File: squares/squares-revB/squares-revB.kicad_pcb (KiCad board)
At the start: 2 copper layers, 113.3 x 75.4 mm, 108 parts, among them J1 USB_C_Pwr, J10 Line In, J11 AND, J12 Mix_In, J13 Mix/Line Out, J14 VCA, J15 Filter, J2 Mux In, J3 Mux Sel, J4 ISP, J5 Square Out Hi, J6 Square Out Lo, J7 Sig Out, J8 Line OUT, J9 Line IN, Q1 2N3906, U1 74HC00, U2 40106, U3 74HC00, U4 74HC00, U5 ATtiny2313-20P, U7 MCP602

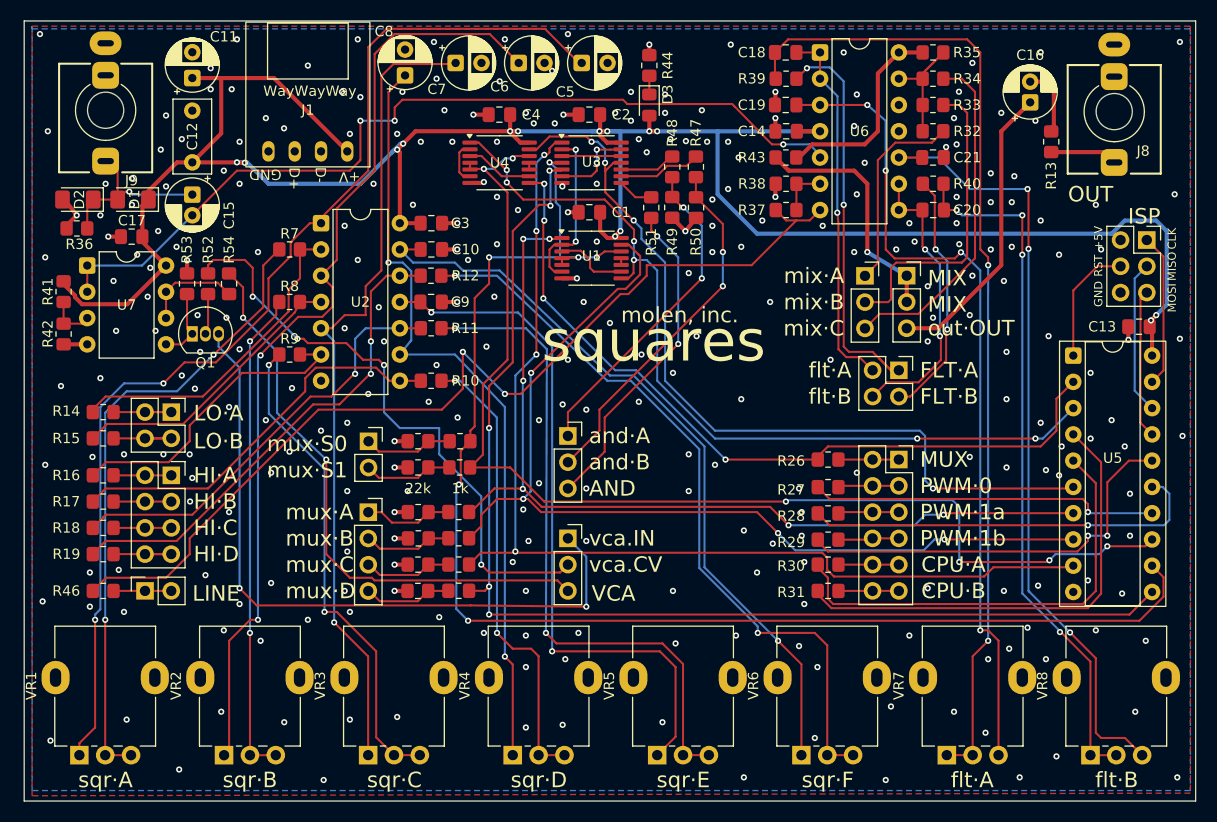
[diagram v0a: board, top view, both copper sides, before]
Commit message: squares: added revB board; added playground firmware
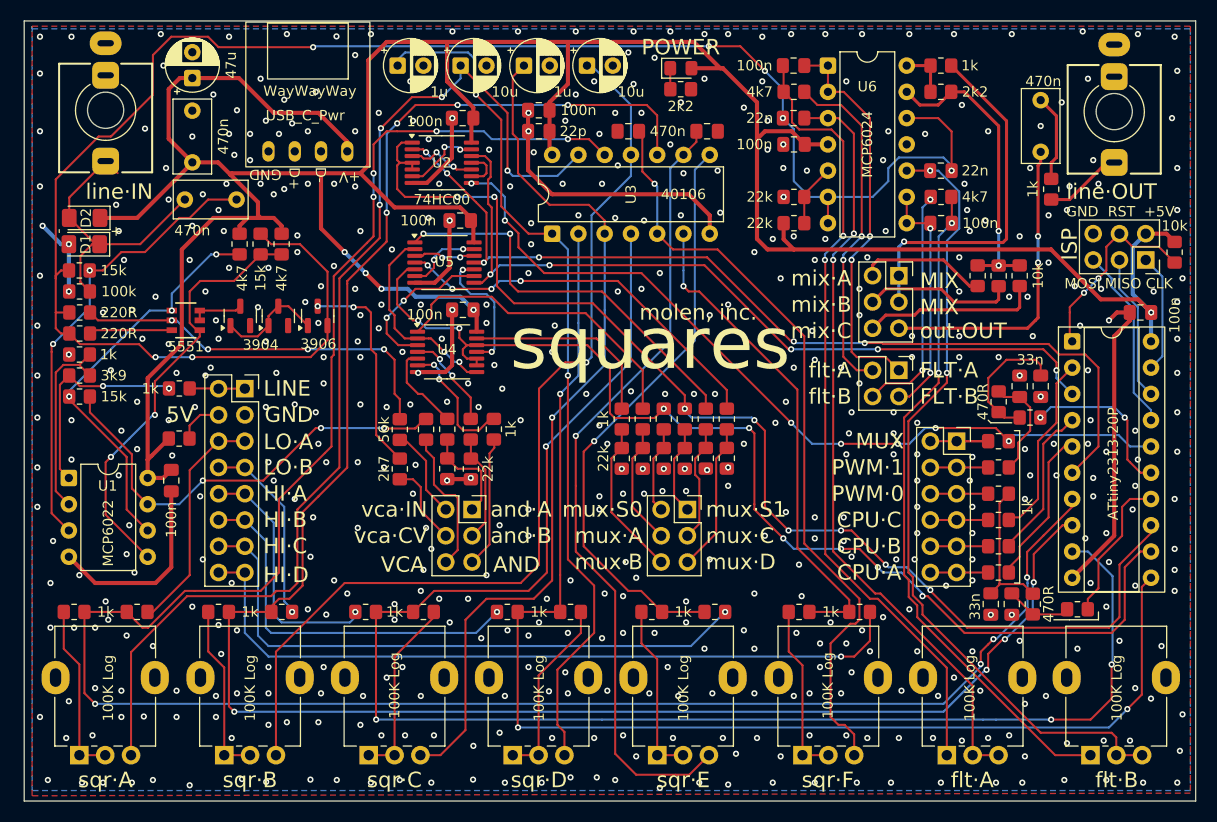
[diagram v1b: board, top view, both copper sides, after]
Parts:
- removed the J10 at (91.4, 75.7)
- removed J11: AND, Connector_PinSocket_2.54mm:PinSocket_1x03_P2.54mm_Vertical
- removed J12: Mix_In, Connector_PinSocket_2.54mm:PinSocket_1x03_P2.54mm_Vertical
- removed J13: Mix/Line Out, Connector_PinSocket_2.54mm:PinSocket_1x03_P2.54mm_Vertical
- removed J14: VCA, Connector_PinSocket_2.54mm:PinSocket_1x03_P2.54mm_Vertical
- removed the J2 at (113.0, 68.1)
- removed the J6 at (94.0, 58.4)
- removed the R2 at (121.8, 70.6)
- removed the R20 at (117.8, 63.8)
- removed the R21 at (117.8, 61.2)
- removed the R25 at (117.9, 68.1)
- removed the R5 at (121.9, 61.2)
- removed the U7 at (85.9, 44.2)
- added C11: 100n, Capacitor_SMD:C_0805_2012Metric_Pad1.18x1.45mm_HandSolder, F.Cu at (129.5, 29.2)
- added C21: 33n, Capacitor_SMD:C_0805_2012Metric_Pad1.18x1.45mm_HandSolder, F.Cu at (178.1, 55.9)
- added C22: 33n, Capacitor_SMD:C_0805_2012Metric_Pad1.18x1.45mm_HandSolder, F.Cu at (176.0, 55.9)
- added C25: 33n, Capacitor_SMD:C_0805_2012Metric_Pad1.18x1.45mm_HandSolder, F.Cu at (175.3, 77.0)
- added C26: 33n, Capacitor_SMD:C_0805_2012Metric_Pad1.18x1.45mm_HandSolder, F.Cu at (173.2, 77.0)
- added J4: VCA, Connector_PinSocket_2.54mm:PinSocket_2x03_P2.54mm_Vertical, F.Cu at (123.1, 67.8)
- added J7: MUX, Connector_PinSocket_2.54mm:PinSocket_2x03_P2.54mm_Vertical, F.Cu at (143.9, 67.8)
- added Q2: 3904, Package_TO_SOT_SMD:SOT-23, F.Cu at (104.3, 49.1)
- added Q3: 3904, Package_TO_SOT_SMD:SOT-23, F.Cu at (100.7, 49.1)
- added Q4: 3906, Package_TO_SOT_SMD:SOT-23, F.Cu at (108.1, 49.1)
- added R10: 15k, Resistor_SMD:R_0805_2012Metric_Pad1.20x1.40mm_HandSolder, F.Cu at (102.6, 42.1)
- added R11: 22k, Resistor_SMD:R_0805_2012Metric_Pad1.20x1.40mm_HandSolder, F.Cu at (94.7, 61.0)
- added R12: 4k7, Resistor_SMD:R_0805_2012Metric_Pad1.20x1.40mm_HandSolder, F.Cu at (104.6, 42.1)
- added R18: 1k, Resistor_SMD:R_0805_2012Metric_Pad1.20x1.40mm_HandSolder, F.Cu at (139.6, 59.1)
- added R19: 1k, Resistor_SMD:R_0805_2012Metric_Pad1.20x1.40mm_HandSolder, F.Cu at (137.5, 59.1)
- added R22: 22k, Resistor_SMD:R_0805_2012Metric_Pad1.20x1.40mm_HandSolder, F.Cu at (139.6, 62.9)
- added R24: 22k, Resistor_SMD:R_0805_2012Metric_Pad1.20x1.40mm_HandSolder, F.Cu at (137.5, 62.9)
- added R3: 15k, Resistor_SMD:R_0805_2012Metric_Pad1.20x1.40mm_HandSolder, F.Cu at (85.1, 44.7)
- added R39: 22k, Resistor_SMD:R_0805_2012Metric_Pad1.20x1.40mm_HandSolder, F.Cu at (141.6, 62.9)
- added R4: 220R, Resistor_SMD:R_0805_2012Metric_Pad1.20x1.40mm_HandSolder, F.Cu at (85.1, 48.8)
- added R40: 1k, Resistor_SMD:R_0805_2012Metric_Pad1.20x1.40mm_HandSolder, F.Cu at (141.6, 59.1)
- added R55: 470R, Resistor_SMD:R_0805_2012Metric_Pad1.20x1.40mm_HandSolder, F.Cu at (177.0, 58.9)
- added R56: 470R, Resistor_SMD:R_0805_2012Metric_Pad1.20x1.40mm_HandSolder, F.Cu at (174.0, 57.4)
- added R58: 10k, Resistor_SMD:R_0805_2012Metric_Pad1.20x1.40mm_HandSolder, F.Cu at (191.0, 42.9)
- added R62: 470R, Resistor_SMD:R_0805_2012Metric_Pad1.20x1.40mm_HandSolder, F.Cu at (177.3, 77.0)
- added R64: 470R, Resistor_SMD:R_0805_2012Metric_Pad1.20x1.40mm_HandSolder, F.Cu at (181.6, 77.5)
- added R7: 15k, Resistor_SMD:R_0805_2012Metric_Pad1.20x1.40mm_HandSolder, F.Cu at (85.1, 56.9)
- added R9: 4k7, Resistor_SMD:R_0805_2012Metric_Pad1.20x1.40mm_HandSolder, F.Cu at (100.6, 42.1)
- added U1: MCP6022, Package_DIP:DIP-8_W7.62mm, F.Cu at (84.1, 64.8)
- C10: renamed from C4; value 100n -> 22p
- C16: renamed from C9; value 100n -> 470n
- C18: value 22n -> 100n
- C19: renamed from C16; value 10u BP -> 470n; footprint Capacitor_THT:CP_Radial_D5.0mm_P2.00mm -> Capacitor_THT:C_Rect_L7.0mm_W3.5mm_P5.00mm
- C2: renamed from C15; value 10u BP -> 470n; footprint Capacitor_THT:CP_Radial_D5.0mm_P2.00mm -> Capacitor_THT:C_Rect_L7.0mm_W3.5mm_P5.00mm
- C24: renamed from C20; value 22n -> 100n
- C9: renamed from C10; value 100n -> 470n
- D3: value LED -> POWER
- J3: value Mux Sel -> Inputs; footprint Connector_PinSocket_2.54mm:PinSocket_1x02_P2.54mm_Vertical -> Connector_PinSocket_2.54mm:PinSocket_2x08_P2.54mm_Vertical
- J5: value Square Out Hi -> MIX; footprint Connector_PinSocket_2.54mm:PinSocket_2x04_P2.54mm_Vertical -> Connector_PinSocket_2.54mm:PinSocket_2x03_P2.54mm_Vertical
- Q1: value 2N3906 -> DMMT5551; footprint Package_TO_SOT_THT:TO-92_Inline -> DMMT5551:SOIC6_DMMT551_DIO
- R1: value 1k -> 220R
- R20: renamed from R52; value 10k -> 56k
- R31: renamed from R53; value 1k -> 2k7
- R34: renamed from R39; value 100k -> 4k7
- R50: renamed from R40; value 100k -> 4k7
- U6: value ~ -> MCP6024
- moved R47 73.4 mm to (160.5, 77.7)
- moved J5 73.0 mm to (164.3, 45.2)
- moved R33 71.9 mm to (154.2, 37.6), turned to 180 degrees
- moved R42 70.9 mm to (154.2, 40.1), turned to 180 degrees
- moved R5 70.3 mm to (85.1, 52.8)
- moved R2 70.2 mm to (85.1, 54.9)
- moved R48 59.7 mm to (146.5, 77.7)
- moved R46 48.2 mm to (154.7, 77.7), turned to 180 degrees
- moved R8 40.8 mm to (84.6, 77.7)
- moved R1 40.5 mm to (85.1, 50.8)
- moved R30 40.5 mm to (126.5, 77.7), turned to 0 degrees
- moved R26 35.0 mm to (120.7, 60.1)
- moved R28 34.9 mm to (120.7, 63.9)
- moved R45 34.8 mm to (140.4, 77.7), turned to 180 degrees
- moved R43 32.5 mm to (147.7, 62.9), turned to 90 degrees
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- renumbered C12 to C1, C2 to C12, C1 to C13, C3 to C14, C19 to C15, C14 to C17, C21 to C20, C13 to C23, C11 to C3, C17 to C4, C6 to C5, C7 to C6, C8 to C7, C5 to C8, D2 to D1, D1 to D2, J9 to J1, J7 to J10, J1 to J2, J15 to J6, J4 to J9, R46 to R13, R15 to R14, R16 to R15, R8 to R16, R14 to R17, R37 to R2, R51 to R21, R48 to R23, R54 to R25, R47 to R26, R10 to R27, R50 to R28, R49 to R29, R17 to R30, R9 to R32, R42 to R33, R44 to R35, R6 to R36, R3 to R37, R23 to R38, R24 to R41, R41 to R42, R22 to R43, R4 to R44, R11 to R45, R12 to R46, R19 to R47, R18 to R48, R13 to R49, R38 to R5, R43 to R51, R35 to R52, R33 to R53, R32 to R54, R34 to R57, R26 to R59, R36 to R6, R28 to R60, R27 to R61, R29 to R63, R30 to R65, R31 to R66, R7 to R8, U4 to U2, U2 to U3, U1 to U4, U3 to U5, U5 to U7
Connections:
- net Net-(J11-Pin_1) renamed AND_b
- net Net-(J11-Pin_2) renamed AND_a
- C15 pad 1: GND -> REF_2.5v
- C16 pad 2: Net-(C9-Pad2) -> Net-(C16-Pad2)
- C2 pad 2: REF_2.5v -> Net-(U1A-+)
- C20 pad 1: GND -> REF_2.5v
- C24 pad 1: Net-(C20-Pad1) -> Net-(C24-Pad1)
- C5 pad 1: Net-(C6-Pad1) -> Net-(C5-Pad1)
- C6 pad 1: Net-(C7-Pad1) -> Net-(C6-Pad1)
- C7 pad 1: Net-(C8-Pad1) -> Net-(C7-Pad1)
- C8 pad 1: Net-(C5-Pad1) -> Net-(C8-Pad1)
- C9 pad 2: Net-(C10-Pad2) -> Net-(C9-Pad2)
- J3 pad 2: Net-(J3-Pin_2) -> Net-(J3-Pin_1)
- J5 pad 2: Net-(J5-Pin_1) -> MIX_In_A
- J5 pad 3: Net-(J5-Pin_3) -> Net-(J5-Pin_1)
- J5 pad 4: Net-(J5-Pin_3) -> MIX_In_B
- J5 pad 5: Net-(J5-Pin_5) -> LINE_Out
- J5 pad 6: Net-(J5-Pin_5) -> MIX_In_C
- J6 pad 1: FILT_A_In -> FILT_A_Out
- J6 pad 2: FILT_A_Out -> FILT_A_In
- J6 pad 3: FILT_B_In -> FILT_B_Out
- J6 pad 4: FILT_B_Out -> FILT_B_In
- Q1 pad 1: Net-(Q1-E) -> Net-(U1B--)
- Q1 pad 3: VCA_in -> Net-(Q1-Pad3)
- R1 pad 1: MUX_In_A -> Net-(Q1-Pad3)
- R1 pad 2: Net-(J2-Pin_1) -> REF_2.5v
- R13 pad 2: Net-(J10-Pin_1) (its old number) -> Net-(J3-Pin_1)
- R14 pad 1: Net-(J6-Pin_3) -> Net-(J3-Pin_7)
- R15 pad 1: Net-(J5-Pin_1) -> Net-(J3-Pin_10)
- R16 pad 2: Net-(R8-Pad2) -> Net-(R16-Pad2)
- R17 pad 1: Net-(J6-Pin_1) -> Net-(J3-Pin_5)
- R2 pad 2: Net-(U6B--) -> Net-(U1A--)
- R20 pad 2: VCA_cv -> VCA_in
- R21 pad 1: Net-(J11-Pin_3) -> AND_out
- R21 pad 2: Net-(R51-Pad2) -> Net-(R21-Pad2)
- R23 pad 1: Net-(R48-Pad1) -> Net-(R23-Pad1)
- R26 pad 1: Net-(R47-Pad1) -> Net-(R26-Pad1)
- R27 pad 2: Net-(R10-Pad2) -> Net-(R27-Pad2)
- R30 pad 1: Net-(J5-Pin_3) -> Net-(J3-Pin_11)
- R31 pad 1: Net-(Q1-E) -> VCA_cv
- R31 pad 2: GND -> Net-(Q4-E)
- R32 pad 2: Net-(R9-Pad2) -> Net-(R32-Pad2)
- R33 pad 1: Net-(U7A-+) -> Net-(U6B-+)
- R36 pad 2: Net-(J3-Pin_2) -> Net-(J7-Pin_1)
- R41 pad 2: Net-(J2-Pin_2) -> Net-(J7-Pin_1)
- R42 pad 1: Net-(U7A-+) -> Net-(U6B-+)
- R45 pad 2: Net-(R11-Pad2) -> Net-(R45-Pad2)
- R46 pad 2: Net-(R12-Pad2) -> Net-(R46-Pad2)
- R47 pad 1: Net-(J5-Pin_7) -> Net-(J3-Pin_15)
- R48 pad 1: Net-(J5-Pin_5) -> Net-(J3-Pin_13)
- R5 pad 2: Net-(U6B--) -> Net-(U1A--)
- R50 pad 1: Net-(C20-Pad1) -> Net-(C24-Pad1)
- R51 pad 2: Net-(J13-Pin_1) -> Net-(J5-Pin_1)
- R60 pad 2: CPU_PWM_1A -> CPU_PWM_0
- R61 pad 2: CPU_PWM_0 -> CPU_PWM_1
- R63 pad 2: CPU_PWM_1B -> CPU_Out_C
- R65 pad 2: CPU_Out_A -> CPU_Out_B
- R66 pad 2: CPU_Out_B -> CPU_Out_A
- R8 pad 2: Net-(R7-Pad2) -> Net-(R8-Pad2)
- U2 pad 1: MUX_Partial_AB -> MUX_Sel1
- U2 pad 10: Net-(U4-Pad10) -> Net-(U2-Pad10)
- U2 pad 11: Net-(U4-Pad10) -> Net-(U2-Pad11)
- U2 pad 12: MUX_Sel1 -> MUX_Partial_AB
- U2 pad 13: MUX_Partial_CD -> Net-(U2-Pad13)
- U2 pad 2: Net-(U4-Pad2) -> MUX_Partial_CD
- U2 pad 3: Net-(U4-Pad3) -> Net-(U2-Pad10)
- U2 pad 6: Net-(U4-Pad2) -> Net-(U2-Pad13)
- U2 pad 9: Net-(U4-Pad3) -> Net-(U2-Pad11)
- U3 pad 1: Net-(C5-Pad1) -> Net-(C7-Pad1)
- U3 pad 10: SqrE_Out -> SqrB_Out
- U3 pad 11: Net-(C9-Pad2) -> Net-(C5-Pad1)
- U3 pad 12: SqrF_Out -> SqrA_Out
- U3 pad 13: Net-(C10-Pad2) -> Net-(C8-Pad1)
- U3 pad 2: SqrA_Out -> SqrD_Out
- U3 pad 4: SqrB_Out -> SqrC_Out
- U3 pad 5: Net-(C7-Pad1) -> Net-(C9-Pad2)
- U3 pad 6: SqrC_Out -> SqrF_Out
- U3 pad 8: SqrD_Out -> SqrE_Out
- U3 pad 9: Net-(C8-Pad1) -> Net-(C16-Pad2)
- U4 pad 10: Net-(U1-Pad10) -> MUX_Sel0
- U4 pad 11: Net-(U1-Pad10) -> Net-(U4-Pad11)
- U4 pad 2: Net-(U1-Pad2) -> Net-(U4-Pad2)
- U4 pad 3: Net-(U1-Pad3) -> Net-(U4-Pad3)
- U4 pad 4: MUX_Sel0 -> Net-(R23-Pad1)
- U4 pad 5: MUX_Sel0 -> Net-(R26-Pad1)
- U4 pad 6: Net-(U1-Pad2) -> Net-(R21-Pad2)
- U4 pad 8: MUX_Partial_AB -> Net-(U4-Pad2)
- U4 pad 9: Net-(U1-Pad3) -> MUX_Sel0
- U5 pad 10: Net-(R48-Pad1) -> Net-(U4-Pad11)
- U5 pad 2: Net-(U1-Pad2) -> Net-(U4-Pad2)
- U5 pad 4: MUX_Sel0 -> MUX_In_D
- U5 pad 5: MUX_In_D -> MUX_Sel0
- U5 pad 8: Net-(R51-Pad2) -> MUX_Partial_AB
- U5 pad 9: Net-(R47-Pad1) -> Net-(U4-Pad3)
- U6 pad 12: GND -> REF_2.5v
- U6 pad 5: REF_2.5v -> Net-(U6B-+)
- U6 pad 6: Net-(U6B--) -> REF_2.5v
- U6 pad 7: LINE_In -> REF_2.5v
- U7 pad 11: MUX_In_D -> SqrD_Out
- U7 pad 14: CPU_PWM_0 -> Net-(U7-PB2)
- U7 pad 15: CPU_PWM_1A -> Net-(U7-PB3)
- U7 pad 16: CPU_PWM_1B -> MUX_Out
- U7 pad 2: MUX_Out -> CPU_Out_C
- U7 pad 7: MUX_In_A -> SqrA_Out
- U7 pad 8: MUX_In_B -> SqrB_Out
- U7 pad 9: MUX_In_C -> SqrC_Out
- VR1 pad 1: Net-(C5-Pad1) -> Net-(R8-Pad2)
- VR1 pad 2: Net-(R7-Pad2) -> Net-(R8-Pad2)
- VR1 pad 3: Net-(R7-Pad2) -> Net-(C8-Pad1)
- VR2 pad 1: Net-(C6-Pad1) -> Net-(R16-Pad2)
- VR2 pad 2: Net-(R8-Pad2) -> Net-(R16-Pad2)
- VR2 pad 3: Net-(R8-Pad2) -> Net-(C5-Pad1)
- VR3 pad 1: Net-(C7-Pad1) -> Net-(R32-Pad2)
- VR3 pad 2: Net-(R9-Pad2) -> Net-(R32-Pad2)
- VR3 pad 3: Net-(R9-Pad2) -> Net-(C6-Pad1)
- VR4 pad 1: Net-(C8-Pad1) -> Net-(R27-Pad2)
- VR4 pad 2: Net-(R10-Pad2) -> Net-(R27-Pad2)
- VR4 pad 3: Net-(R10-Pad2) -> Net-(C7-Pad1)
- VR5 pad 1: Net-(C9-Pad2) -> Net-(R46-Pad2)
- VR5 pad 2: Net-(R11-Pad2) -> Net-(R46-Pad2)
- VR5 pad 3: Net-(R11-Pad2) -> Net-(C9-Pad2)
- VR6 pad 1: Net-(C10-Pad2) -> Net-(R45-Pad2)
- VR6 pad 2: Net-(R12-Pad2) -> Net-(R45-Pad2)
- VR6 pad 3: Net-(R12-Pad2) -> Net-(C16-Pad2)
- VR7 pad 2: Net-(C18-Pad1) -> Net-(U6A-+)
- VR8 pad 1: Net-(C20-Pad1) -> Net-(C24-Pad1)
- VR8 pad 2: Net-(C20-Pad1) -> Net-(U6C-+)
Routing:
- net SqrA_Out: track 31.6 -> 207.2 mm, vias 0 -> 8
- net SqrB_Out: track 27.7 -> 189.5 mm, vias 0 -> 8
- net SqrC_Out: track 30.0 -> 153.5 mm, vias 0 -> 4
- net REF_2.5v: track 85.5 -> 180.2 mm, vias 3 -> 7
- net SqrD_Out: track 38.4 -> 125.9 mm, vias 0 -> 3
- net Net-(C16-Pad2): track 0.00 -> 77.3 mm, vias 0 -> 1
- net MUX_In_D: track 114.6 -> 37.7 mm, vias 5 -> 4
- net MUX_In_B: track 95.2 -> 19.4 mm, vias 4 -> 0
- net +5V: track 228.4 -> 303.2 mm, vias 14 -> 5
- net LINE_In: track 94.9 -> 21.1 mm
- net GND: track 38.8 -> 112.5 mm, vias 285 -> 525
- net Net-(J3-Pin_15): track 0.00 -> 73.2 mm, vias 0 -> 1
- net Net-(C10-Pad2): track 72.9 -> 0.00 mm, vias 1 -> 0
- net Net-(R12-Pad2): track 72.2 -> 0.00 mm, vias 2 -> 0
- net Net-(C20-Pad1): track 67.8 -> 0.00 mm, vias 4 -> 0
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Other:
- board text added: "+"
- board text added: "-"
- board text added: "5V"
- board text added: "CPU·C"
- board text added: "PWM·1"
- board text added: "let's try that again"
- board text added: "line·IN"
- board text added: "line·OUT"
- board text added: "rev·B"
- board text added: "vca·CV"
- board text added: "vca·IN"
- board text removed: "OUT"
- board text removed: "PWM·1a"
- board text removed: "PWM·1b"
- board text removed: "vca.CV"
- board text removed: "vca.IN"

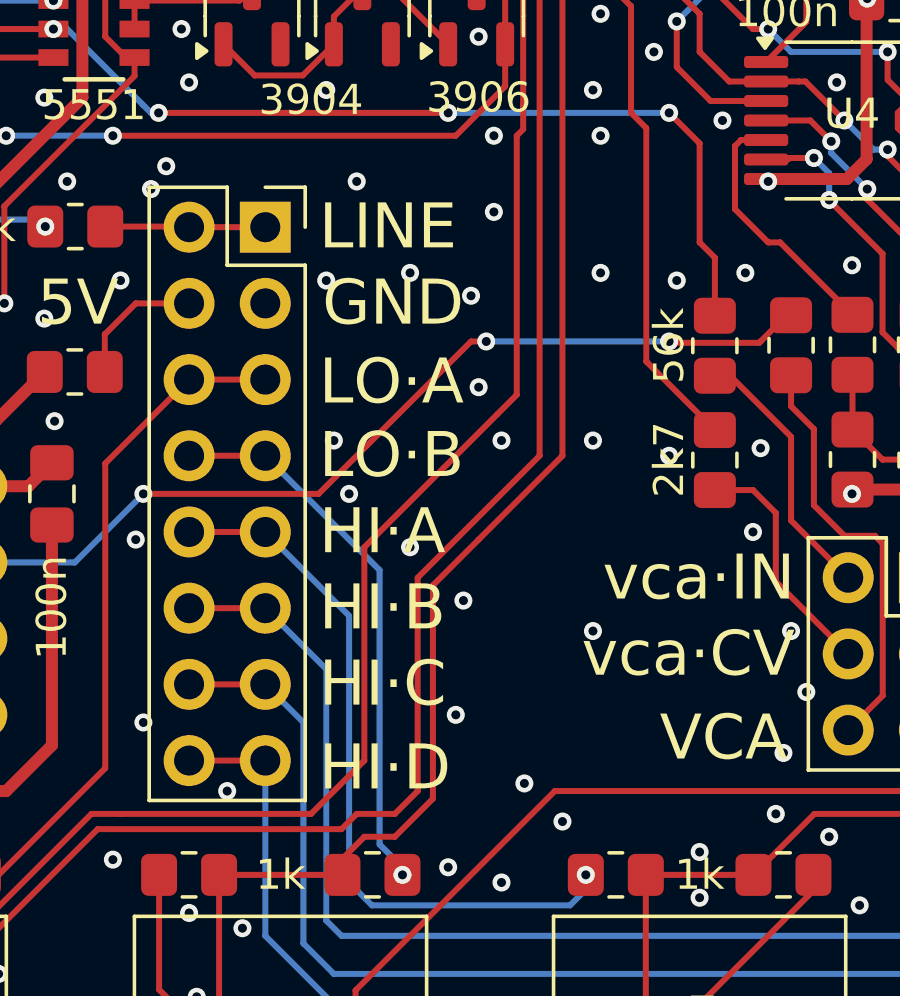
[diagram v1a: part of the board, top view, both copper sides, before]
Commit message: [squares] PWM_A is now lil percussive env triggered by MUX_Sel0
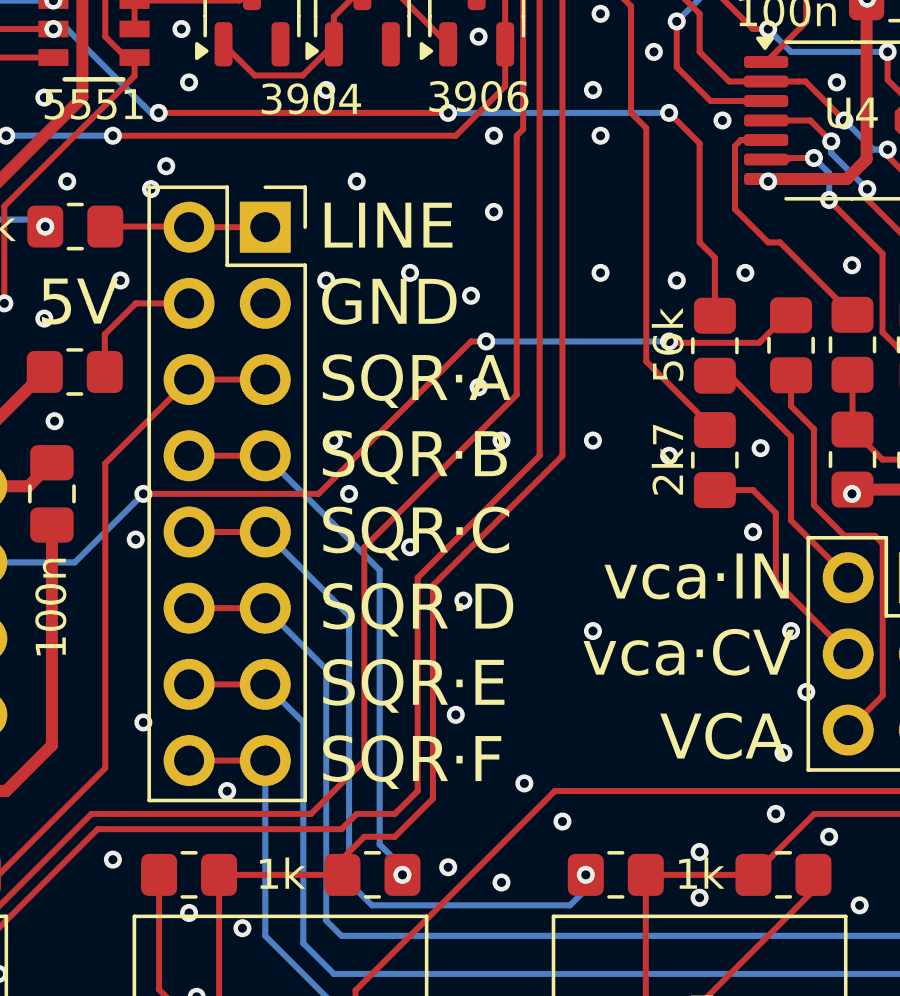
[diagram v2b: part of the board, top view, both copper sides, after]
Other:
- board text added: "SQR·A"
- board text added: "SQR·B"
- board text added: "SQR·C"
- board text added: "SQR·D"
- board text added: "SQR·E"
- board text added: "SQR·F"
- board text removed: "HI·A"
- board text removed: "HI·B"
- board text removed: "HI·C"
- board text removed: "HI·D"
- board text removed: "LO·A"
- board text removed: "LO·B"
